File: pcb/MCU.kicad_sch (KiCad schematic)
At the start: 28 parts, among them J2 TC2030, J3 Conn_01x02_Pin, U2 LM4040DBZ-3, U6 FM24C64B, U7 STM32H563VITx, Y1 3225-25M-SR

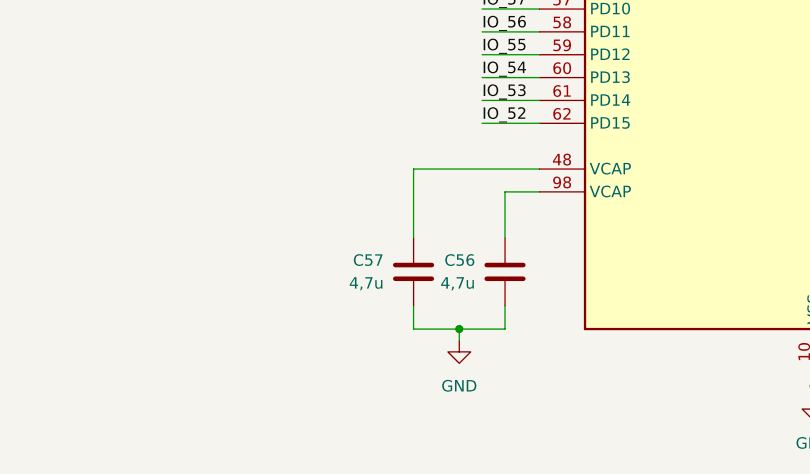
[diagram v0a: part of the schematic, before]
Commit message: Unify component values/footprints per checklist; add via-in-pad DRC rule; regenerate production outputs
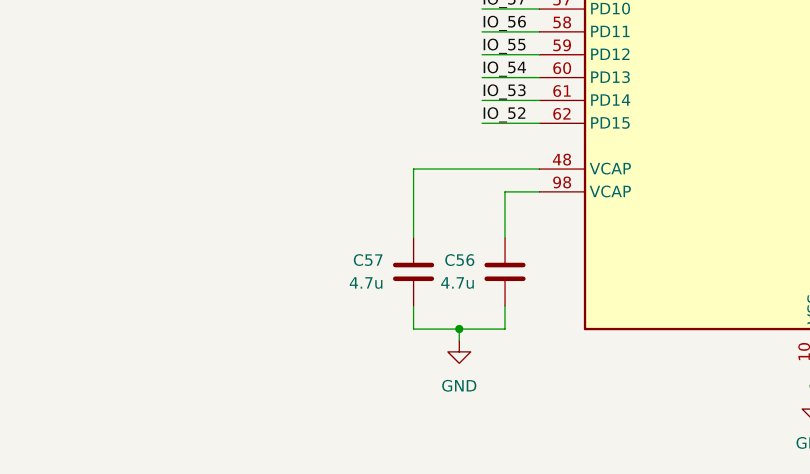
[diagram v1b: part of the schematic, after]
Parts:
- C27, C29, C35, C39, C49, C50, C53, C54, C55, C58: footprint Capacitor_SMD:C_0603_1608Metric_Pad1.08x0.95mm_HandSolder -> Capacitor_SMD:C_0603_1608Metric
- C51: footprint Capacitor_SMD:C_1206_3216Metric_Pad1.33x1.80mm_HandSolder -> Capacitor_SMD:C_1206_3216Metric
- C56, C57: value 4,7u -> 4.7u; footprint Capacitor_SMD:C_0603_1608Metric_Pad1.08x0.95mm_HandSolder -> Capacitor_SMD:C_0603_1608Metric
- R21, R84, R85: footprint Resistor_SMD:R_0603_1608Metric_Pad0.98x0.95mm_HandSolder -> Resistor_SMD:R_0603_1608Metric
- R80: footprint Resistor_SMD:R_0402_1005Metric_Pad0.72x0.64mm_HandSolder -> Resistor_SMD:R_0402_1005Metric

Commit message: Apply review checklist fixes, add fiducials, regenerate production outputs
- W5500 clock from MCU MCO1 by default (R80 fitted, R23 DNP)
- Firmware .ioc: I2C1_SCL moved to PB8 to match schematic
- 2 fiducials per side (hand assembly), zones refilled
- Restore DRC exclusions dropped from .kicad_pro on last save (59, unchanged set)
- README: status updated (ready for prototype order), renders and production links
- .gitignore: drop leftover RDE_board ibom.config.ini entry
- Regenerate BOM, PDFs, gerber zip, interactive BOM and 3D renders
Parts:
- C19, C20: now fitted
- Y1: now fitted; now left out of the parts list
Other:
- moved on the sheet: C27, C29, C35, C39, C49, C50, C51, C53, C54, C55, C56, C57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

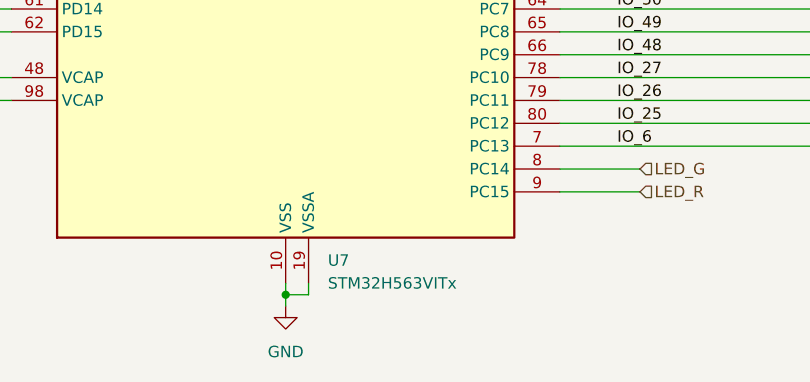
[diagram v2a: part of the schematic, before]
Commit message: Fix BOM data: 0603 LED part number (D1/D2/D4/D6/D13/D14), BOM field cleanup
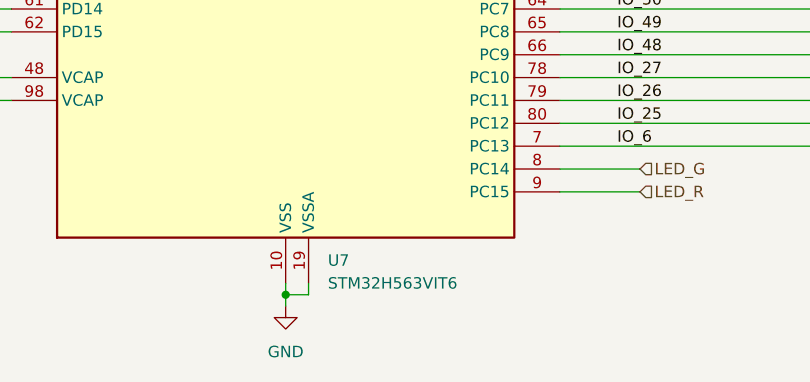
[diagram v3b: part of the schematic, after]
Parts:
- U7: value STM32H563VITx -> STM32H563VIT6
